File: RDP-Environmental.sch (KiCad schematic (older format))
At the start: 31 parts, among them J1 OPENLOG, J2 MPU, J3 RT1, J4 RT2, J5 RT3, J6 RT4, J7 3.3V, J8 AVR-PDI-6, U1 MS5607, U2 ATxmega32A4U-AU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

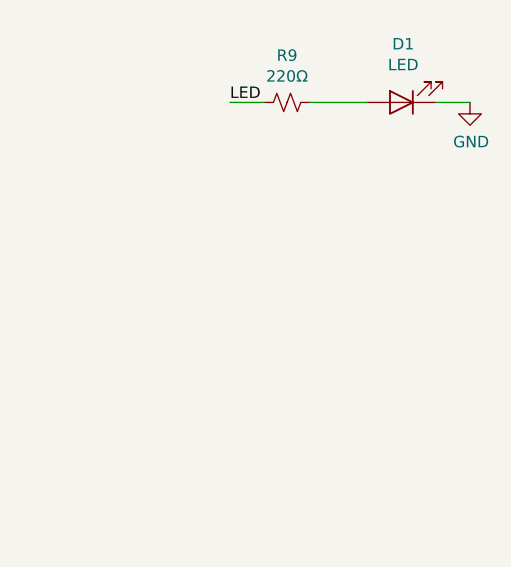
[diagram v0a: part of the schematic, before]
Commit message: Add GPS and groud to output for FPGA
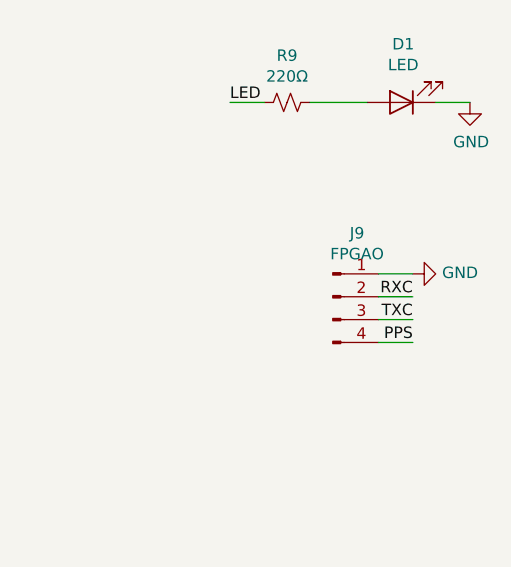
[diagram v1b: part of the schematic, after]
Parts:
- added J9: FPGAO, Connector_Molex:Molex_KK-254_AE-6410-04A_1x04_P2.54mm_Vertical, symbol Connector:Conn_01x04_Male
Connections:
- net GND: now also J9.1 (Pin_1)
- net PPS: now also J9.4 (Pin_4)
- net RXC: now also J9.2 (Pin_2)
- net TXC: now also J9.3 (Pin_3)
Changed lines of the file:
@@
 Text Label 5150 5950 2    50   ~ 0
 TXC
+$Comp
+L Connector:Conn_01x04_Male J9
+U 1 1 5BD834D6
+P 9650 2250
+F 0 "J9" H 9756 2528 50  0000 C CNN
+F 1 "FPGAO" H 9756 2437 50  0000 C CNN
+F 2 "Connector_Molex:Molex_KK-254_AE-6410-04A_1x04_P2.54mm_Vertical" H 9650 2250 50  0001 C CNN
+F 3 "~" H 9650 2250 50  0001 C CNN
+	1    9650 2250
+	1    0    0    -1
+$EndComp
+Wire Wire Line
+	9850 2150 10000 2150
+Wire Wire Line
+	9850 2250 10000 2250
+Wire Wire Line
+	10000 2350 9850 2350
+$Comp
+L power:GND #PWR034
+U 1 1 5BD8EC35
+P 10000 2150
+F 0 "#PWR034" H 10000 1900 50  0001 C CNN
+F 1 "GND" V 10005 2022 50  0000 R CNN
+F 2 "" H 10000 2150 50  0001 C CNN
+F 3 "" H 10000 2150 50  0001 C CNN
+	1    10000 2150
+	0    -1   -1   0
+$EndComp
+Text Label 10000 2350 2    50   ~ 0
+TXC
+Text Label 10000 2250 2    50   ~ 0
+RXC
+Wire Wire Line
+	10000 2450 9850 2450
+Text Label 10000 2450 2    50   ~ 0
+PPS
 $EndSCHEMATC

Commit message: Fix MPU 9250 clearance
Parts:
- U1: symbol MS560702BA03-50:MS560702BA03-50 -> RDP-Environmental-rescue:MS560702BA03-50-MS560702BA03-50
- U3: symbol RDP-Environmental:CAM-M8Q-0 -> RDP-Environmental-rescue:CAM-M8Q-0-RDP-Environmental
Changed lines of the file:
@@
 $EndComp
 $Comp
-L MS560702BA03-50:MS560702BA03-50 U1
+L RDP-Environmental-rescue:MS560702BA03-50-MS560702BA03-50 U1
 U 1 1 5BD34A0F
 P 3350 1200
@@
 	1700 4600 2000 4600
 $Comp
-L RDP-Environmental:CAM-M8Q-0 U3
+L RDP-Environmental-rescue:CAM-M8Q-0-RDP-Environmental U3
 U 1 1 5BD655C5
 P 6150 1650

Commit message: Fix thermistor resistance values
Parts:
- R1, R2, R3, R4: value 200Ω -> 50kΩ
- U1: symbol RDP-Environmental-rescue:MS560702BA03-50-MS560702BA03-50 -> RDP-Environmental-rescue:MS560702BA03-50-MS560702BA03-50-RDP-Environmental-rescue
- U3: symbol RDP-Environmental-rescue:CAM-M8Q-0-RDP-Environmental -> RDP-Environmental-rescue:CAM-M8Q-0-RDP-Environmental-RDP-Environmental-rescue
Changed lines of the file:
@@
 $EndComp
 $Comp
-L RDP-Environmental-rescue:MS560702BA03-50-MS560702BA03-50 U1
+L RDP-Environmental-rescue:MS560702BA03-50-MS560702BA03-50-RDP-Environmental-rescue U1
 U 1 1 5BD34A0F
 P 3350 1200
@@
 	1700 4600 2000 4600
 $Comp
-L RDP-Environmental-rescue:CAM-M8Q-0-RDP-Environmental U3
+L RDP-Environmental-rescue:CAM-M8Q-0-RDP-Environmental-RDP-Environmental-rescue U3
 U 1 1 5BD655C5
 P 6150 1650
@@
 P 2200 4000
 F 0 "R4" V 1995 4000 50  0000 C CNN
-F 1 "200Ω" V 2086 4000 50  0000 C CNN
+F 1 "50kΩ" V 2086 4000 50  0000 C CNN
 F 2 "Resistor_SMD:R_0805_2012Metric_Pad1.15x1.40mm_HandSolder" H 2200 4000 50  0001 C CNN
 F 3 "~" H 2200 4000 50  0001 C CNN
@@
 P 2200 3650
 F 0 "R3" V 1995 3650 50  0000 C CNN
-F 1 "200Ω" V 2086 3650 50  0000 C CNN
+F 1 "50kΩ" V 2086 3650 50  0000 C CNN
 F 2 "Resistor_SMD:R_0805_2012Metric_Pad1.15x1.40mm_HandSolder" H 2200 3650 50  0001 C CNN
 F 3 "~" H 2200 3650 50  0001 C CNN
@@
 P 2200 3300
 F 0 "R2" V 1995 3300 50  0000 C CNN
-F 1 "200Ω" V 2086 3300 50  0000 C CNN
+F 1 "50kΩ" V 2086 3300 50  0000 C CNN
 F 2 "Resistor_SMD:R_0805_2012Metric_Pad1.15x1.40mm_HandSolder" H 2200 3300 50  0001 C CNN
 F 3 "~" H 2200 3300 50  0001 C CNN
@@
 P 2200 2950
 F 0 "R1" V 1995 2950 50  0000 C CNN
-F 1 "200Ω" V 2086 2950 50  0000 C CNN
+F 1 "50kΩ" V 2086 2950 50  0000 C CNN
 F 2 "Resistor_SMD:R_0805_2012Metric_Pad1.15x1.40mm_HandSolder" H 2200 2950 50  0001 C CNN
 F 3 "~" H 2200 2950 50  0001 C CNN

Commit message: Add status LED pins for GPS and general status
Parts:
- added J10: Environmental, Connector_Molex:Molex_KK-254_AE-6410-02A_1x02_P2.54mm_Vertical, symbol Connector:Conn_01x02_Male
- added J11: GPS, Connector_Molex:Molex_KK-254_AE-6410-02A_1x02_P2.54mm_Vertical, symbol Connector:Conn_01x02_Male
- added R10, R11: R_Small_US, Resistor_SMD:R_0805_2012Metric_Pad1.15x1.40mm_HandSolder, symbol Device:R_Small_US
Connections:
- net GND: now also J10.1 (Pin_1), J11.1 (Pin_1)
- net at U2.5 (PB1): now also R10.2
- net at U2.6 (PB2): now also R11.1
- new net ENV_STAT: J10.2 (Pin_2), R10.1
- new net GPS_STAT: J11.2 (Pin_2), R11.2
- no-connect marks 31 -> 29
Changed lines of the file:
@@
 NoConn ~ 4900 5750
 NoConn ~ 4900 5450
-NoConn ~ 4900 5350
-NoConn ~ 4900 5250
-NoConn ~ 4900 5150
 NoConn ~ 4900 4950
 NoConn ~ 4900 4850
@@
 Text Label 10000 2450 2    50   ~ 0
 PPS
+NoConn ~ 4900 5150
+$Comp
+L Connector:Conn_01x02_Male J10
+U 1 1 5C43CA19
+P 9650 2700
+F 0 "J10" H 9622 2673 50  0000 R CNN
+F 1 "Environmental" H 9622 2582 50  0000 R CNN
+F 2 "Connector_Molex:Molex_KK-254_AE-6410-02A_1x02_P2.54mm_Vertical" H 9650 2700 50  0001 C CNN
+F 3 "~" H 9650 2700 50  0001 C CNN
+	1    9650 2700
+	1    0    0    -1
+$EndComp
+$Comp
+L Connector:Conn_01x02_Male J11
+U 1 1 5C43D0A0
+P 9650 3050
+F 0 "J11" H 9622 3023 50  0000 R CNN
+F 1 "GPS" H 9622 2932 50  0000 R CNN
+F 2 "Connector_Molex:Molex_KK-254_AE-6410-02A_1x02_P2.54mm_Vertical" H 9650 3050 50  0001 C CNN
+F 3 "~" H 9650 3050 50  0001 C CNN
+	1    9650 3050
+	1    0    0    -1
+$EndComp
+Text Label 5850 5250 2    50   ~ 0
+ENV_STAT
+Text Label 5850 5350 2    50   ~ 0
+GPS_STAT
+Wire Wire Line
+	10000 2700 9850 2700
+Wire Wire Line
+	10000 3050 9850 3050
+Wire Wire Line
+	9850 2800 10150 2800
+Wire Wire Line
+	9850 3150 10150 3150
+$Comp
+L power:GND #PWR0108
+U 1 1 5C45BAEA
+P 10000 2700
+F 0 "#PWR0108" H 10000 2450 50  0001 C CNN
+F 1 "GND" V 10005 2572 50  0000 R CNN
+F 2 "" H 10000 2700 50  0001 C CNN
+F 3 "" H 10000 2700 50  0001 C CNN
+	1    10000 2700
+	0    -1   -1   0
+$EndComp
+$Comp
+L power:GND #PWR0109
+U 1 1 5C45BBD8
+P 10000 3050
+F 0 "#PWR0109" H 10000 2800 50  0001 C CNN
+F 1 "GND" V 10005 2922 50  0000 R CNN
+F 2 "" H 10000 3050 50  0001 C CNN
+F 3 "" H 10000 3050 50  0001 C CNN
+	1    10000 3050
+	0    -1   -1   0
+$EndComp
+Text Label 10150 2800 2    50   ~ 0
+ENV_STAT
+Text Label 10150 3150 2    50   ~ 0
+GPS_STAT
+$Comp
+L Device:R_Small_US R10
+U 1 1 5C5714C1
+P 5350 5250
+F 0 "R10" V 5145 5250 50  0000 C CNN
+F 1 "R_Small_US" V 5236 5250 50  0000 C CNN
+F 2 "Resistor_SMD:R_0805_2012Metric_Pad1.15x1.40mm_HandSolder" H 5350 5250 50  0001 C CNN
+F 3 "~" H 5350 5250 50  0001 C CNN
+	1    5350 5250
+	0    1    1    0
+$EndComp
+$Comp
+L Device:R_Small_US R11
+U 1 1 5C571598
+P 5350 5350
+F 0 "R11" V 5250 5350 50  0000 C CNN
+F 1 "R_Small_US" V 5200 5350 50  0000 C CNN
+F 2 "Resistor_SMD:R_0805_2012Metric_Pad1.15x1.40mm_HandSolder" H 5350 5350 50  0001 C CNN
+F 3 "~" H 5350 5350 50  0001 C CNN
+	1    5350 5350
+	0    -1   -1   0
+$EndComp
+Wire Wire Line
+	5450 5350 5850 5350
+Wire Wire Line
+	5450 5250 5850 5250
+Wire Wire Line
+	4900 5250 5250 5250
+Wire Wire Line
+	4900 5350 5250 5350
 $EndSCHEMATC
